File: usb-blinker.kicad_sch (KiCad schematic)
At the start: 12 parts, among them J1 USB_C_Receptacle_PowerOnly_6P, U1 TLC555xPW

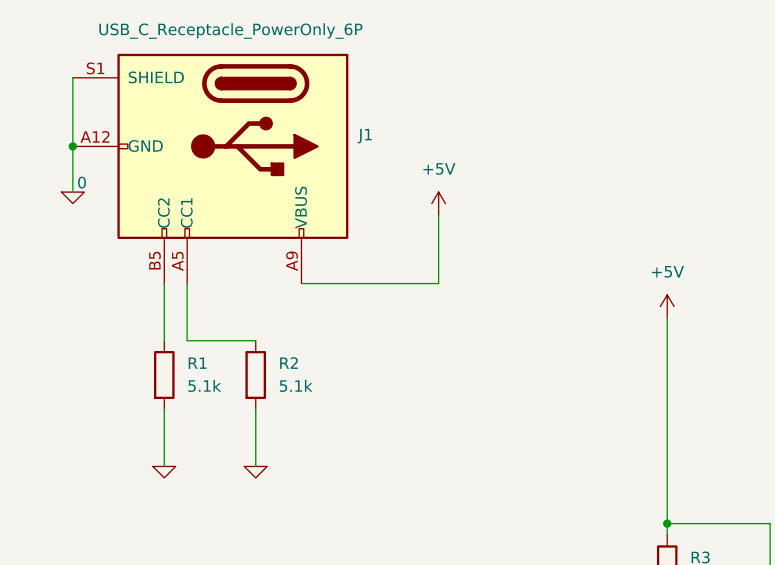
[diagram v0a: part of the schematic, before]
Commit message: added fuse, pcb remake
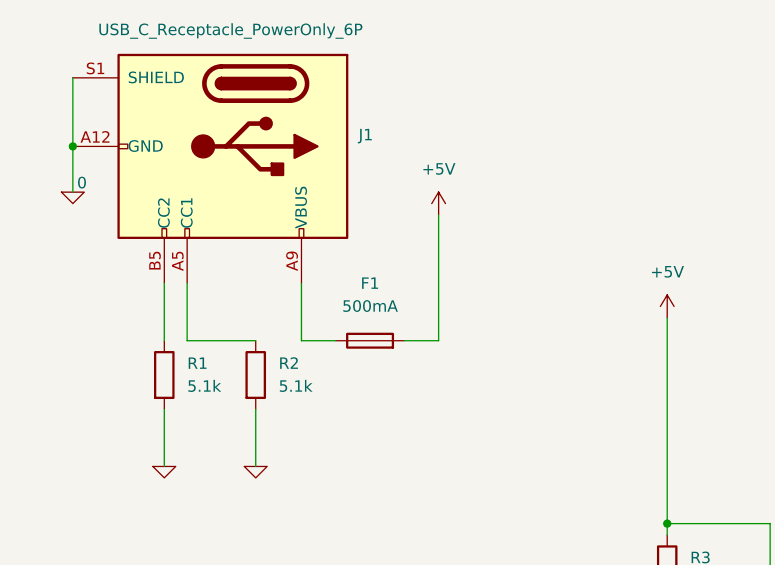
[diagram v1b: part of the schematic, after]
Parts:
- added F1: 500mA, Fuse:Fuse_0603_1608Metric, symbol Device:Fuse
- C1, C2, C3: footprint Capacitor_SMD:C_0201_0603Metric -> Capacitor_SMD:C_0603_1608Metric
- R1, R2, R3, R4, R5: footprint Resistor_SMD:R_0201_0603Metric -> Resistor_SMD:R_0603_1608Metric
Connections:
- net +5V: now also F1.2; no longer J1.A9 (VBUS), J1.B9 (VBUS)
- new net: F1.1, J1.A9 (VBUS), J1.B9 (VBUS)
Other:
- title: (none) -> USB-BLINKER
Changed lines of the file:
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@@
 	(generator_version "9.0")
 	(paper "A4")
+	(title_block
+		(title "USB-BLINKER")
+		(date "2026-03-06")
+	)
 	(junction
 		(at 34.29 38.1)
@@
 	(wire
 		(pts
+			(xy 59.69 59.69) (xy 59.69 53.34)
+		)
+		(stroke
+			(width 0)
+			(type default)
+		)
+	)
+	(wire
+		(pts
 			(xy 46.99 59.69) (xy 54.61 59.69)
 		)
@@
 	(wire
 		(pts
-			(xy 59.69 53.34) (xy 74.93 53.34)
+			(xy 59.69 59.69) (xy 63.5 59.69)
 		)
 		(stroke
@@
 	(wire
 		(pts
-			(xy 74.93 45.72) (xy 74.93 53.34)
+			(xy 74.93 45.72) (xy 74.93 59.69)
 		)
 		(stroke
@@
 		(pts
 			(xy 100.33 109.22) (xy 100.33 116.84)
+		)
+		(stroke
+			(width 0)
+			(type default)
+		)
+	)
+	(wire
+		(pts
+			(xy 71.12 59.69) (xy 74.93 59.69)
 		)
 		(stroke
@@
 			)
 		)
-		(property "Footprint" "Resistor_SMD:R_0201_0603Metric"
+		(property "Footprint" "Resistor_SMD:R_0603_1608Metric"
 			(at 52.832 63.5 90)
 			(effects
@@
 			)
 		)
-		(property "Footprint" "Capacitor_SMD:C_0201_0603Metric"
+		(property "Footprint" "Capacitor_SMD:C_0603_1608Metric"
 			(at 101.2952 109.22 0)
 			(effects
@@
 			)
 		)
-		(property "Footprint" "Resistor_SMD:R_0201_0603Metric"
+		(property "Footprint" "Resistor_SMD:R_0603_1608Metric"
 			(at 98.552 85.09 90)
 			(effects
@@
 			)
 		)
-		(property "Footprint" "Capacitor_SMD:C_0201_0603Metric"
+		(property "Footprint" "Capacitor_SMD:C_0603_1608Metric"
 			(at 117.8052 76.2 0)
 			(effects
@@
 			)
 		)
-		(property "Footprint" "Resistor_SMD:R_0201_0603Metric"
+		(property "Footprint" "Resistor_SMD:R_0603_1608Metric"
 			(at 42.672 63.5 90)
 			(effects
@@
 			)
 		)
-		(property "Footprint" "Resistor_SMD:R_0201_0603Metric"
+		(property "Footprint" "Resistor_SMD:R_0603_1608Metric"
 			(at 153.162 80.01 90)
 			(effects
@@
 			)
 		)
-		(property "Footprint" "Resistor_SMD:R_0201_0603Metric"
+		(property "Footprint" "Resistor_SMD:R_0603_1608Metric"
 			(at 98.552 95.25 90)
 			(effects
@@
 			)
 		)
-		(property "Footprint" "Capacitor_SMD:C_0201_0603Metric"
+		(property "Footprint" "Capacitor_SMD:C_0603_1608Metric"
 			(at 138.7348 68.58 0)
 			(effects
@@
 					(unit 1)
 				)
+			)
+		)
+	)
+	(symbol
+		(lib_id "Device:Fuse")
+		(at 67.31 59.69 90)
+		(unit 1)
+		(exclude_from_sim no)
+		(in_bom yes)
+		(on_board yes)
+		(dnp no)
+		(fields_autoplaced yes)
+		(property "Reference" "F1"
+			(at 67.31 53.34 90)
+			(effects
+				(font
+					(size 1.27 1.27)
+				)
+			)
+		)
+		(property "Value" "500mA"
+			(at 67.31 55.88 90)
+			(effects
+				(font
+					(size 1.27 1.27)
+				)
+			)
+		)
+		(property "Footprint" "Fuse:Fuse_0603_1608Metric"
+			(at 67.31 61.468 90)
+			(effects
+				(font
+					(size 1.27 1.27)
+				)
+				(hide yes)
+			)
+		)
+		(property "Datasheet" "~"
+			(at 67.31 59.69 0)
+			(effects
+				(font
+					(size 1.27 1.27)
+				)
+				(hide yes)
+			)
+		)
+		(property "Description" "Fuse"
+			(at 67.31 59.69 0)
+			(effects
+				(font
+					(size 1.27 1.27)
+				)
+				(hide yes)
+			)
+		)
+		(pin "2"
+		)
+		(pin "1"
+		)
+		(instances
+			(project ""
+				(path "/2479fa30-b975-451a-9e65-31b8e812188e"
+					(reference "F1")
+					(unit 1)
+				)

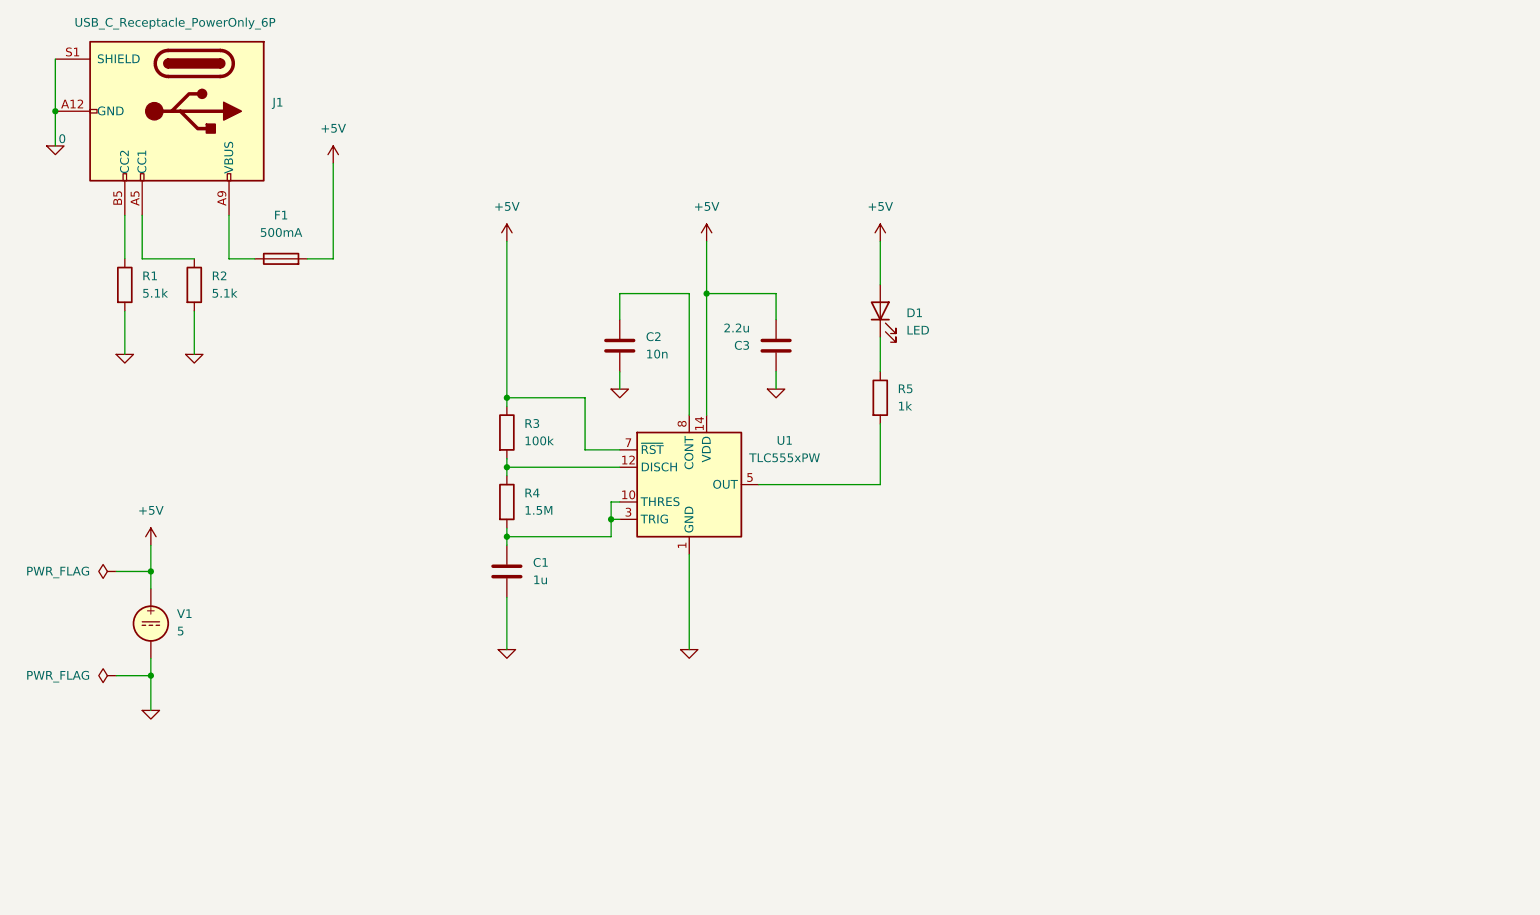
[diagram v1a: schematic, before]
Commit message: wider power traces
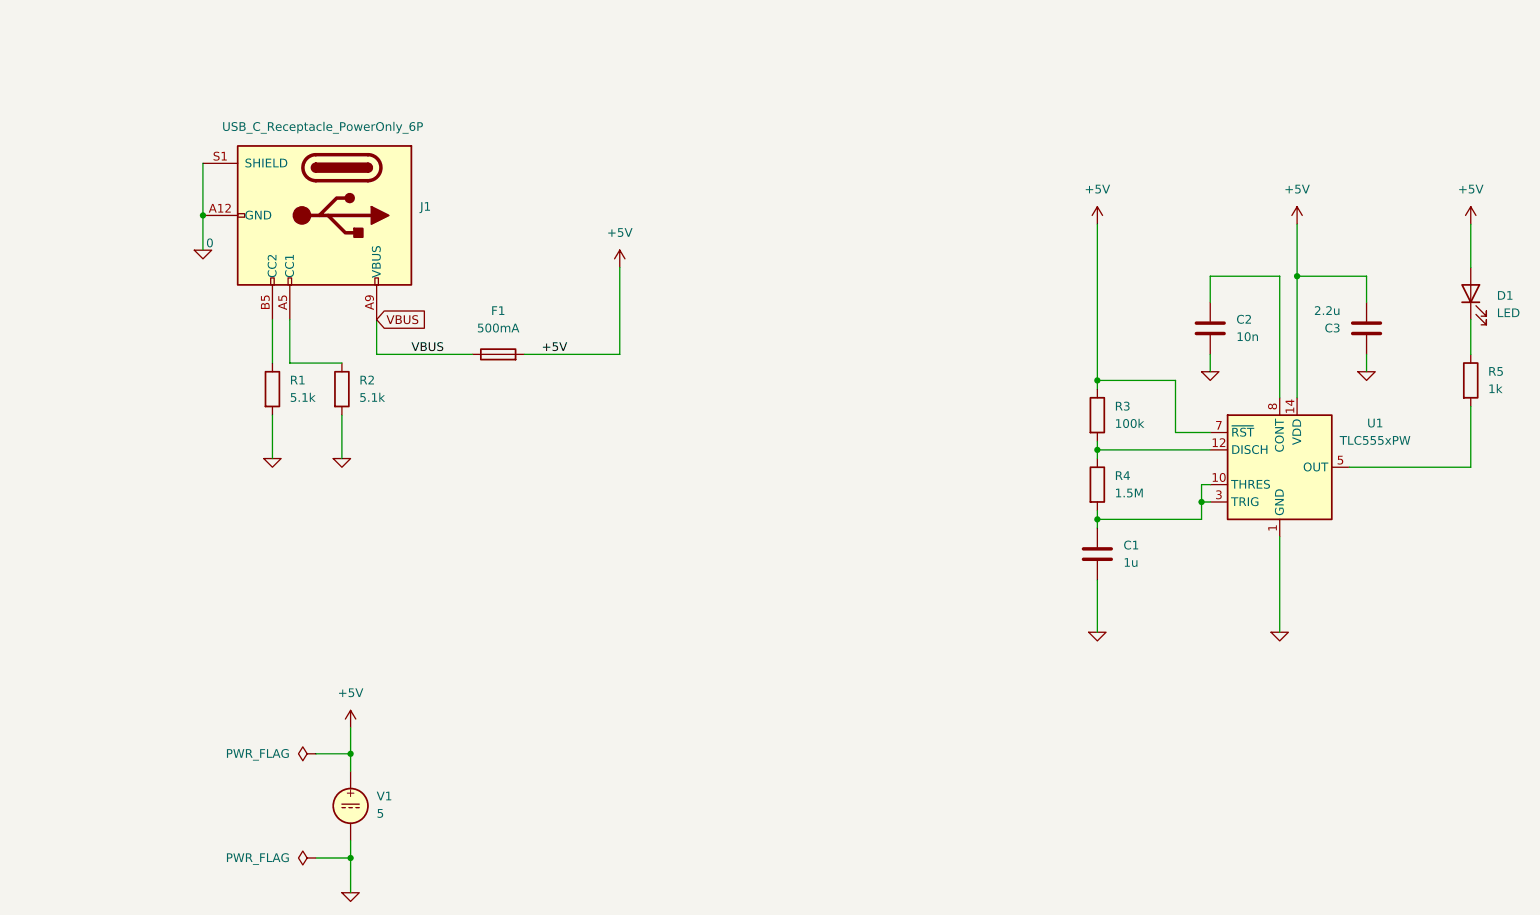
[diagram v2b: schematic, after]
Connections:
- net VBUS: now reaches F1.1, J1.A9 (VBUS), J1.B9 (VBUS)
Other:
- moved on the sheet: C1, C2, C3, D1, F1, J1, R1, R2, R3, R4, R5, U1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
